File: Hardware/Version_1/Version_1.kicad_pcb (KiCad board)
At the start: 6 copper layers, 65 x 30 mm, 108 parts, among them IC1 LIFCL-40-7BG256C, IC2 W25R256JVEIQ, IC3 IS46TR16128D-125KBLA2, IC4 TPS62A01DRLR, IC5 TPS62A01DRLR, IC6 TPS62A01DRLR, J1 Conn_01x02_Pin, J2 Conn_01x05_Pin, J3 52435-2271, J4 52435-2271, J6 GPIO, U1 CAT24C256, Y1 AK3ADDF1-156.2500T3

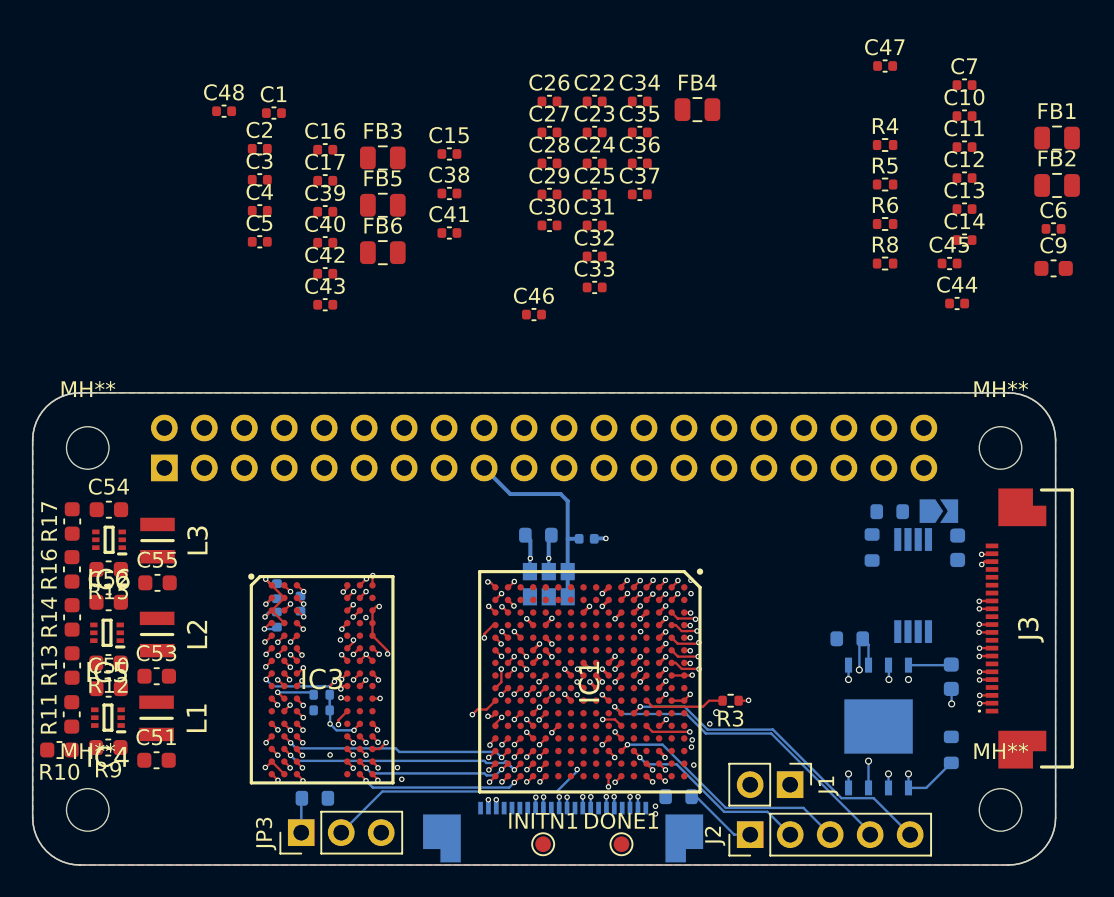
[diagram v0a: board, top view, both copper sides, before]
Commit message: Added decoupling c for DRAM
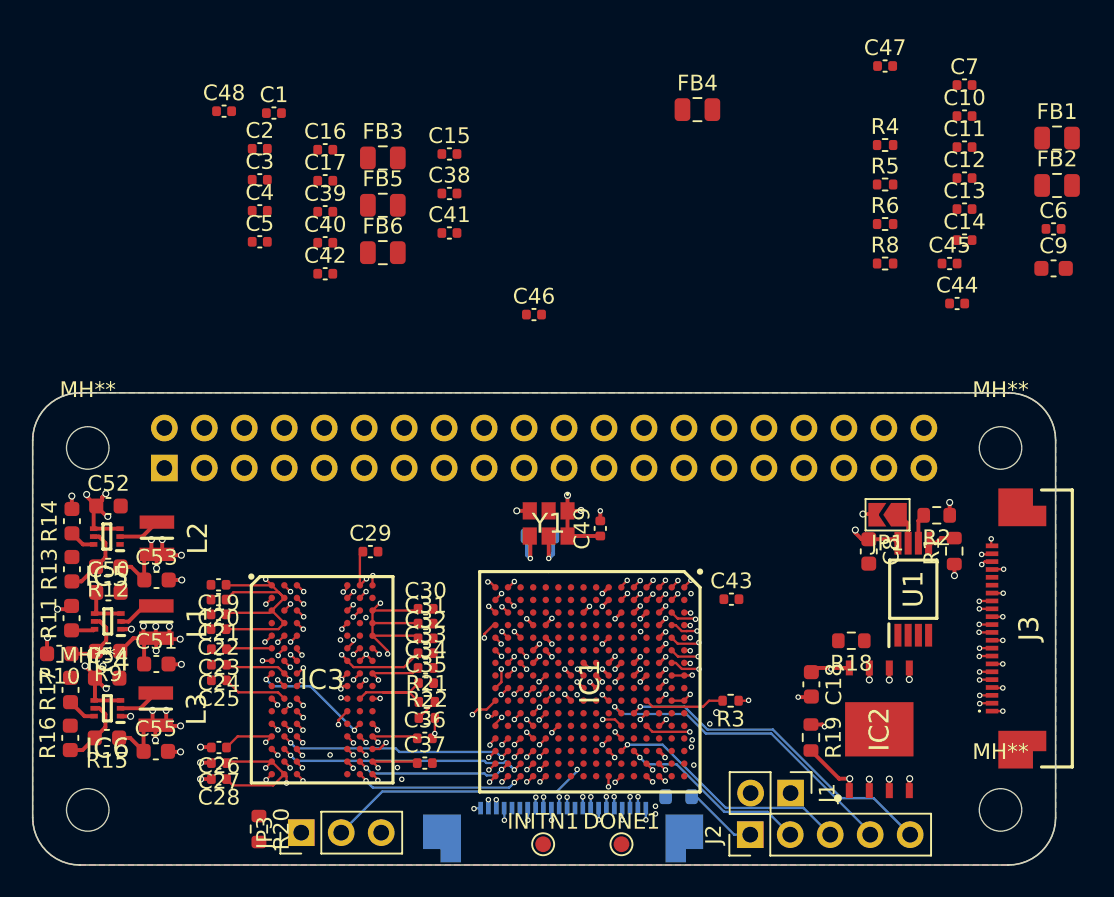
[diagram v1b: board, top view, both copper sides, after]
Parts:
- C18, C19, C20, C21, C49, C8, IC2, JP1, R1, R18, R19, R2, R20, R21, R22, U1, Y1: moved to F.Cu
- moved C26 46.1 mm to (111.8, 92.5), turned to 180 degrees
- moved C27 45.2 mm to (111.8, 93.5), turned to 180 degrees
- moved C28 44.4 mm to (111.8, 94.5), turned to 180 degrees
- moved C22 41.2 mm to (111.8, 85.0), turned to 180 degrees
- moved C23 40.6 mm to (111.8, 86.3), turned to 180 degrees
- moved C24 39.8 mm to (111.8, 87.3), turned to 180 degrees
- moved C25 39.0 mm to (111.8, 88.3), turned to 180 degrees
- moved C36 39.0 mm to (124.9, 91.9)
- moved C37 38.6 mm to (124.9, 93.5)
- moved C34 38.5 mm to (125.0, 87.5)
- moved C35 37.5 mm to (125.0, 88.4)
- moved C43 31.9 mm to (144.4, 83.1)
- moved C31 27.5 mm to (125.0, 84.7)
- moved C32 26.5 mm to (125.0, 85.6)
- moved C33 25.6 mm to (125.0, 86.5)
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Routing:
- net /VCCDRAM: track 19.0 -> 80.7 mm, vias 14 -> 12
- net GND: track 32.2 -> 49.1 mm, vias 53 -> 77
- net +5V: track 0.00 -> 15.4 mm, vias 0 -> 6
- net +1V5: track 0.00 -> 12.3 mm, vias 0 -> 6
- net +1V0: track 0.59 -> 10.6 mm, vias 2 -> 7
- net +1V8: track 0.00 -> 9.95 mm, vias 0 -> 4
- net Net-(IC5-FB): track 0.00 -> 4.59 mm
- net Net-(IC6-FB): track 0.00 -> 4.53 mm
- net /MD0: track 15.5 -> 19.9 mm
- net Net-(IC4-FB): track 0.00 -> 4.29 mm
- net /MCSN: track 21.9 -> 18.2 mm
- net Net-(IC5-SW): track 0.00 -> 2.72 mm
- net Net-(IC4-SW): track 0.00 -> 2.66 mm
- net Net-(IC6-SW): track 0.00 -> 2.64 mm
- net Net-(JP3-A): track 2.20 -> 0.00 mm
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- added copper zone on In3.Cu, net +1V0
- added copper zone on In3.Cu, net +1V5
- added copper zone on In3.Cu, net +1V8
- added copper zone on In3.Cu, net +3V3
- added copper zone on In1.Cu, net +5V
- removed copper zone on In3.Cu, net /VCCDRAM
